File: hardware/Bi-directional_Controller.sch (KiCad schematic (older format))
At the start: 58 parts, among them J1 ON/OFF, J13 MOTOR, J14 Serial, J2 Conn_01x06, J3 Conn_02x03_Odd_Even, J7 BAT 12V, J8 CH1, Q1 BSS138, Q10 AOD240, Q12 AO6401A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

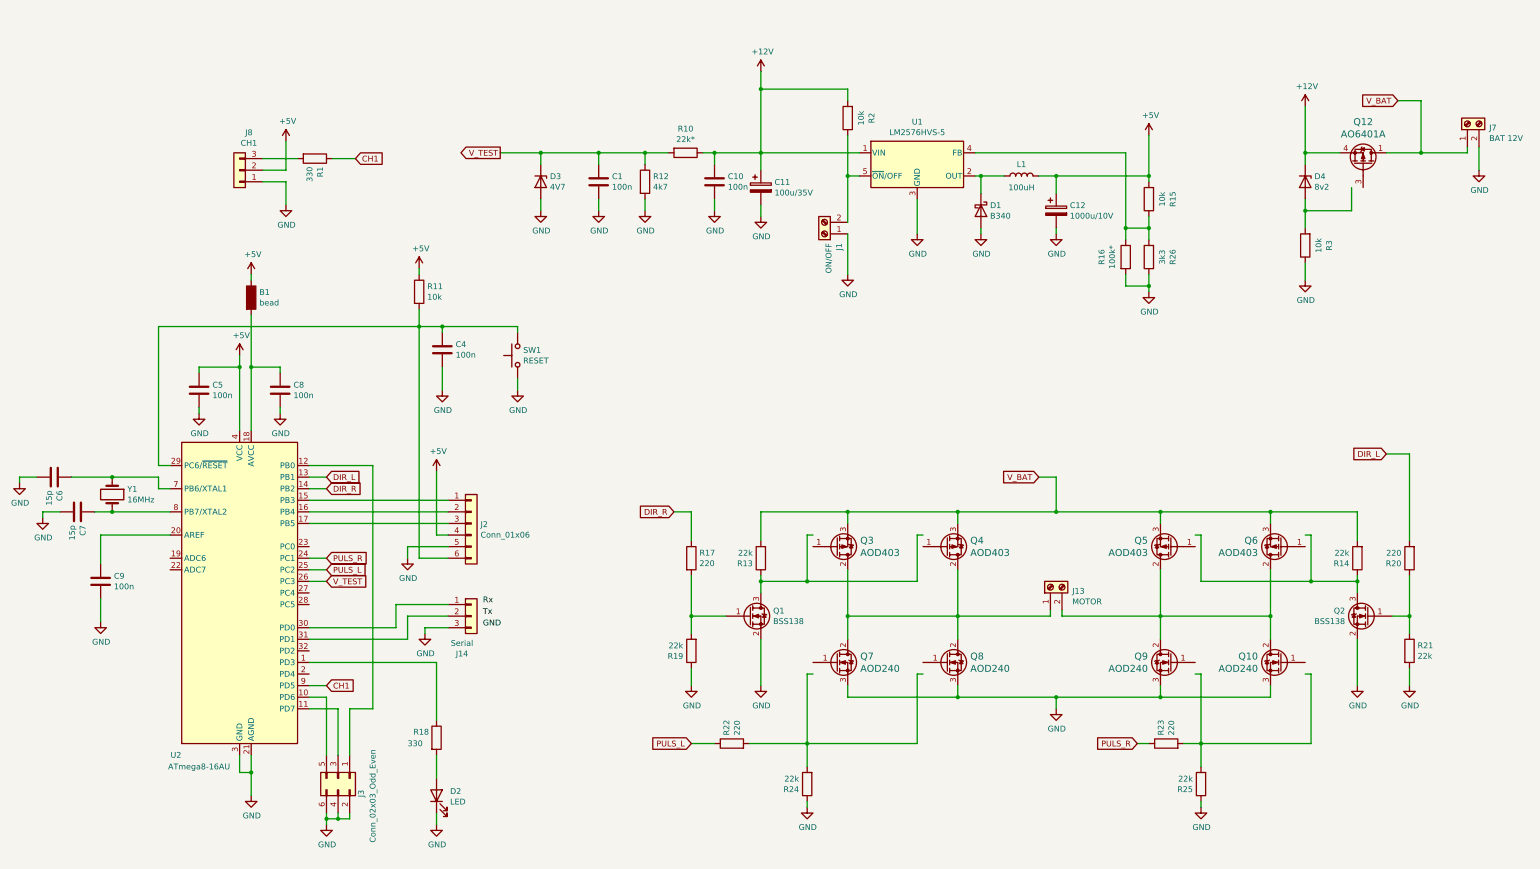
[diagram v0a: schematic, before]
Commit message: symbols update
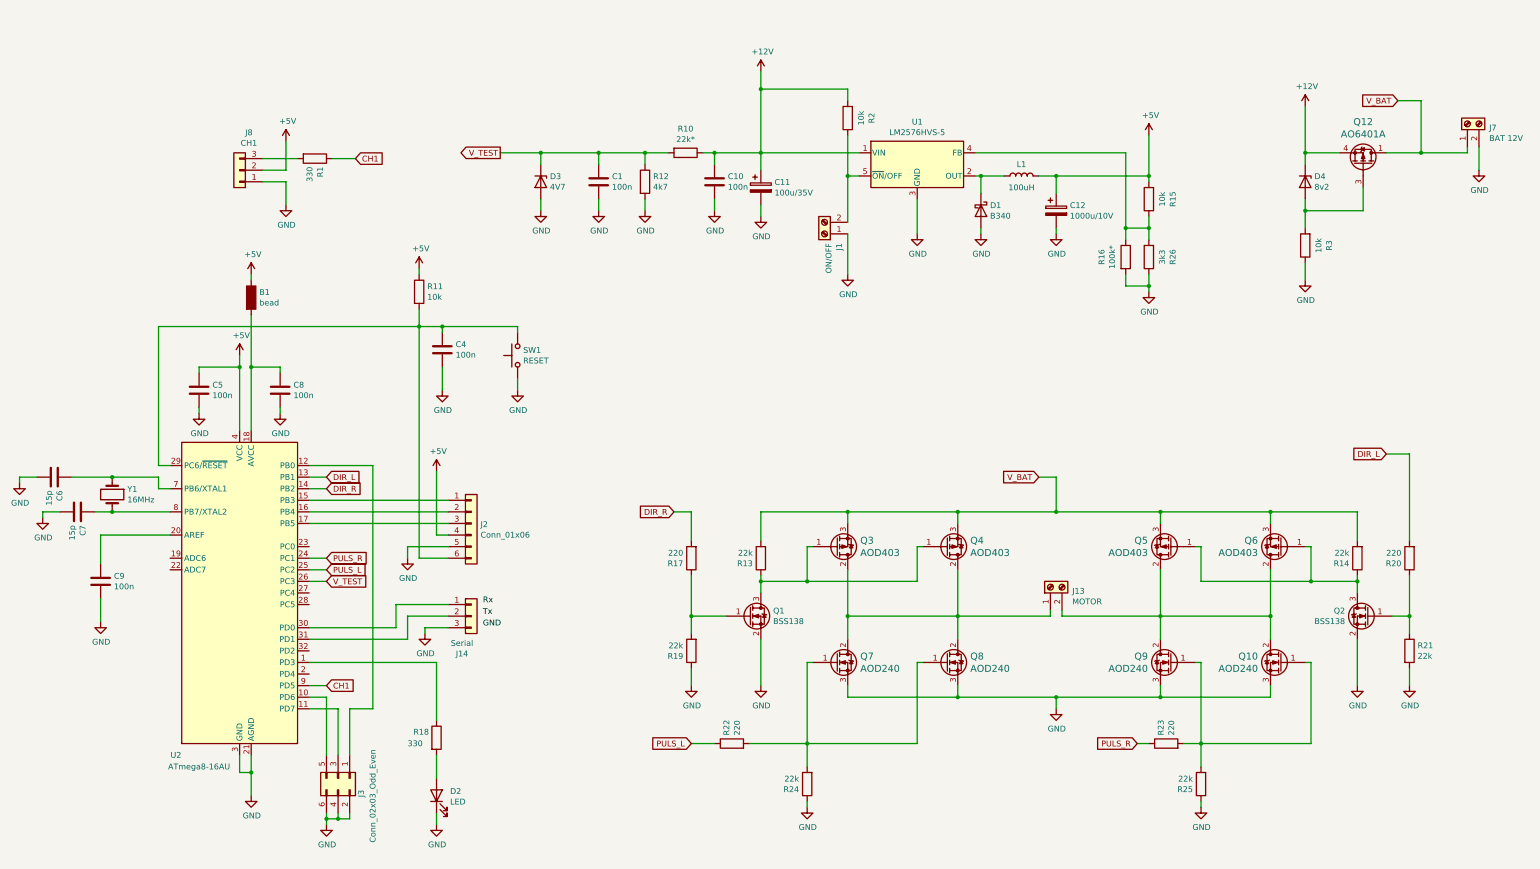
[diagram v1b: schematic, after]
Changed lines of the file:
@@
 	5400 6350 5500 6350
 Wire Wire Line
-	8600 6350 8600 6750
-Wire Wire Line
-	12950 6350 12950 6750
-Wire Wire Line
-	12000 6350 12000 6750
-Wire Wire Line
-	9550 6350 9550 6750
-Wire Wire Line
-	8600 7550 8600 8150
-Wire Wire Line
-	9550 7550 9550 8150
-Wire Wire Line
-	12000 7550 12000 8150
-Wire Wire Line
-	12950 7550 12950 8150
+	8600 6450 8600 6750
+Wire Wire Line
+	12950 6450 12950 6750
+Wire Wire Line
+	12000 6450 12000 6750
+Wire Wire Line
+	9550 6450 9550 6750
+Wire Wire Line
+	8600 7450 8600 8150
+Wire Wire Line
+	9550 7450 9550 8150
+Wire Wire Line
+	12000 7450 12000 8150
+Wire Wire Line
+	12950 7450 12950 8150
 Wire Wire Line
 	10100 3250 10100 3400
@@
 F 3 "~" H 7600 6550 50  0001 C CNN
 	1    7600 6550
-	1    0    0    -1
+	-1   0    0    1
 $EndComp
 Wire Wire Line
@@
 $EndComp
 Wire Wire Line
-	8650 6350 8600 6350
+	8650 6450 8600 6450
 $Comp
 L obbo_Transistors:AOD403 Q4
@@
 $EndComp
 Wire Wire Line
-	9600 6350 9550 6350
+	9600 6450 9550 6450
 $Comp
 L obbo_Transistors:AOD403 Q5
@@
 $EndComp
 Wire Wire Line
-	11950 6350 12000 6350
-Wire Wire Line
-	12950 6350 12900 6350
+	11950 6450 12000 6450
+Wire Wire Line
+	12950 6450 12900 6450
 $Comp
 L obbo_Transistors:AOD240 Q7
@@
 $EndComp
 Wire Wire Line
-	9600 7550 9550 7550
-Wire Wire Line
-	8650 7550 8600 7550
+	9600 7450 9550 7450
+Wire Wire Line
+	8650 7450 8600 7450
 $Comp
 L obbo_Transistors:AOD240 Q9
@@
 $EndComp
 Wire Wire Line
-	12900 7550 12950 7550
-Wire Wire Line
-	11950 7550 12000 7550
+	12900 7450 12950 7450
+Wire Wire Line
+	11950 7450 12000 7450
 $Comp
 L Device:D_Zener D3
@@
 	12900 3550 12900 3450
 Wire Wire Line
-	13300 3550 13300 3350
+	13400 3550 13400 3350
 Wire Wire Line
 	13600 3050 13900 3050
@@
 	12900 3050 13200 3050
 Wire Wire Line
-	12900 3550 13300 3550
+	12900 3550 13400 3550
 Connection ~ 12900 3550
 $Comp

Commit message: support for Atmega328
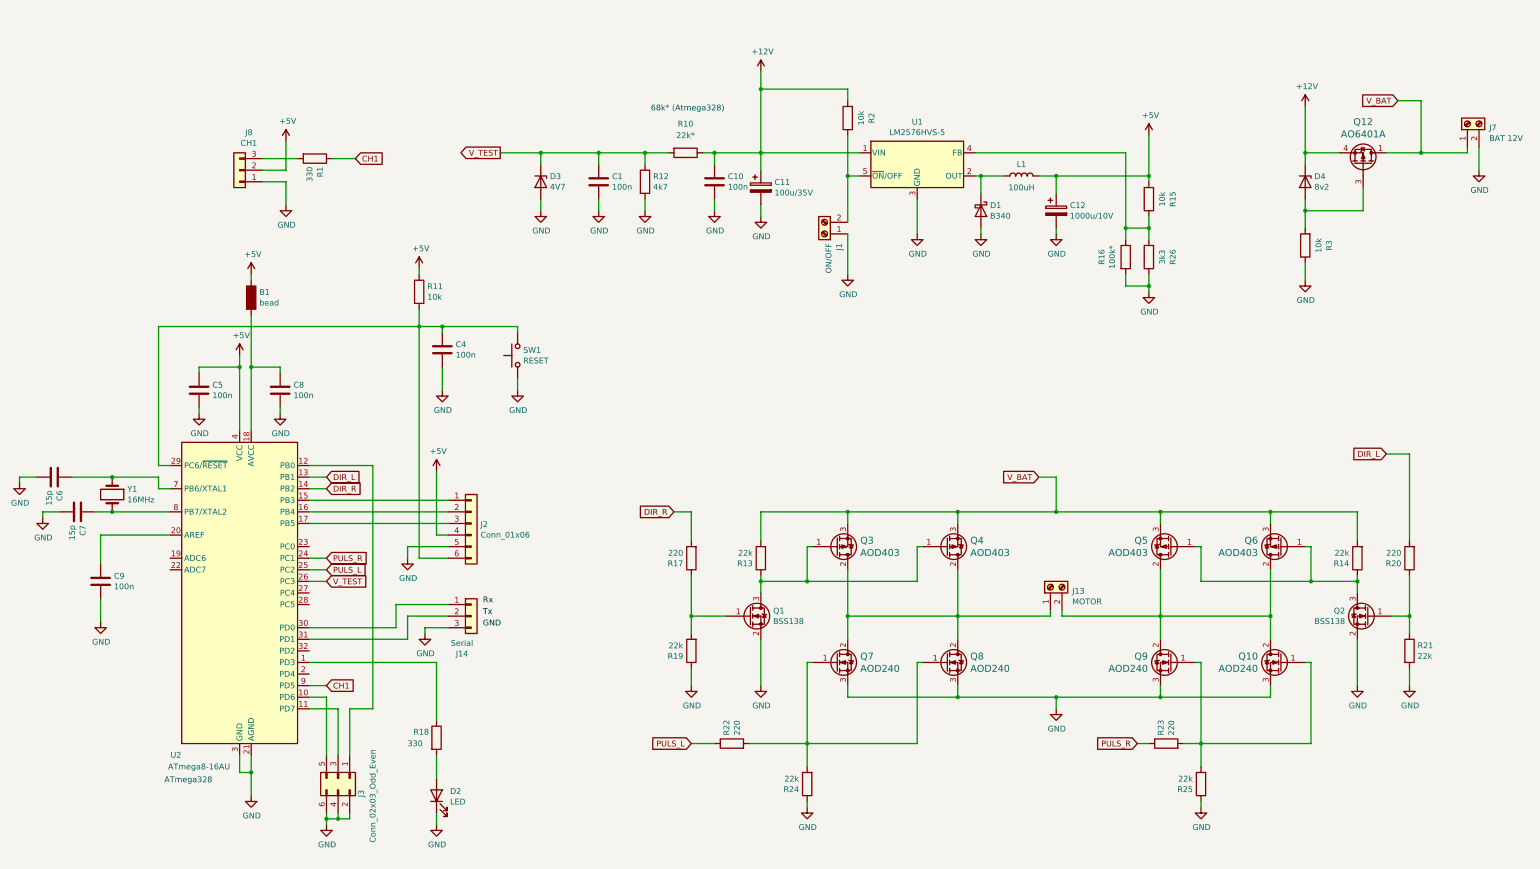
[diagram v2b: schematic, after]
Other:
- note added: "68k* (Atmega328)"
- note added: "ATmega328"
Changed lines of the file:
@@
 U 1 1 5C9FC603
 P 7550 3050
-F 0 "R10" V 7343 3050 50  0000 C CNN
-F 1 "22k*" V 7434 3050 50  0000 C CNN
+F 0 "R10" V 7300 3050 50  0000 C CNN
+F 1 "22k*" V 7400 3050 50  0000 C CNN
 F 2 "obbo_footprints:R_0805K" V 7480 3050 50  0001 C CNN
 F 3 "~" H 7550 3050 50  0001 C CNN
@@
 Text GLabel 4450 6650 2    50   Input ~ 0
 PULS_L
+Text Notes 3050 8500 0    50   ~ 0
+ATmega328
+Text Notes 7250 2700 0    50   ~ 0
+68k* (Atmega328)
 $EndSCHEMATC

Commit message: symbol update
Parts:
- removed Q10, Q7, Q8, Q9: AOD240, obbo_footprints:TO-252-2-DPAK, symbol obbo_Transistors:AOD240
- removed Q12: AO6401A, Package_SO:TSOP-6_1.65x3.05mm_P0.95mm, symbol obbo_Transistors:AO6401A
- removed Q3, Q4, Q5, Q6: AOD403, obbo_footprints:TO-252-2-DPAK, symbol obbo_Transistors:AOD403
- added Q10, Q7, Q8, Q9: AOD240, obbo_footprints:TO-252-2-DPAK, symbol obbo_Transistor:AOD240
- added Q12: AO6401A, Package_SO:TSOP-6_1.65x3.05mm_P0.95mm, symbol obbo_Transistor:AO6401A
- added Q3, Q4, Q5, Q6: AOD403, obbo_footprints:TO-252-2-DPAK, symbol obbo_Transistor:AOD403
- C1, C6, C7, C9: footprint obbo_footprints:C_0805K -> Capacitor_SMD:C_0805_2012Metric
- R1, R10, R11, R12, R13, R14, R15, R17, R18, R2, R20, R24, R25, R3: footprint obbo_footprints:R_0805K -> Resistor_SMD:R_0805_2012Metric
- R16: value 100k* -> 11k*; footprint obbo_footprints:R_0805K -> Resistor_SMD:R_0805_2012Metric
- R26: value 3k3 -> 4k7; footprint obbo_footprints:R_0805K -> Resistor_SMD:R_0805_2012Metric
- U2: footprint Housings_QFP:TQFP-32_7x7mm_Pitch0.8mm -> Package_QFP:TQFP-32_7x7mm_P0.8mm
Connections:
- wire segments 231 -> 236
- no-connect marks 0 -> 7
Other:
- moved on the sheet: J8, R1
